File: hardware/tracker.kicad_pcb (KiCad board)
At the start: 2 copper layers, 27.9 x 40.6 mm, 19 parts, among them P1 Motor, P2 ISP, P3 Logic Power, P4 Motor Power, Q1 IRML9301TRPbF, SW1 Direction, SW2 Speed, U1 MC78L05A, U2 ATTINY85, U3 A4988

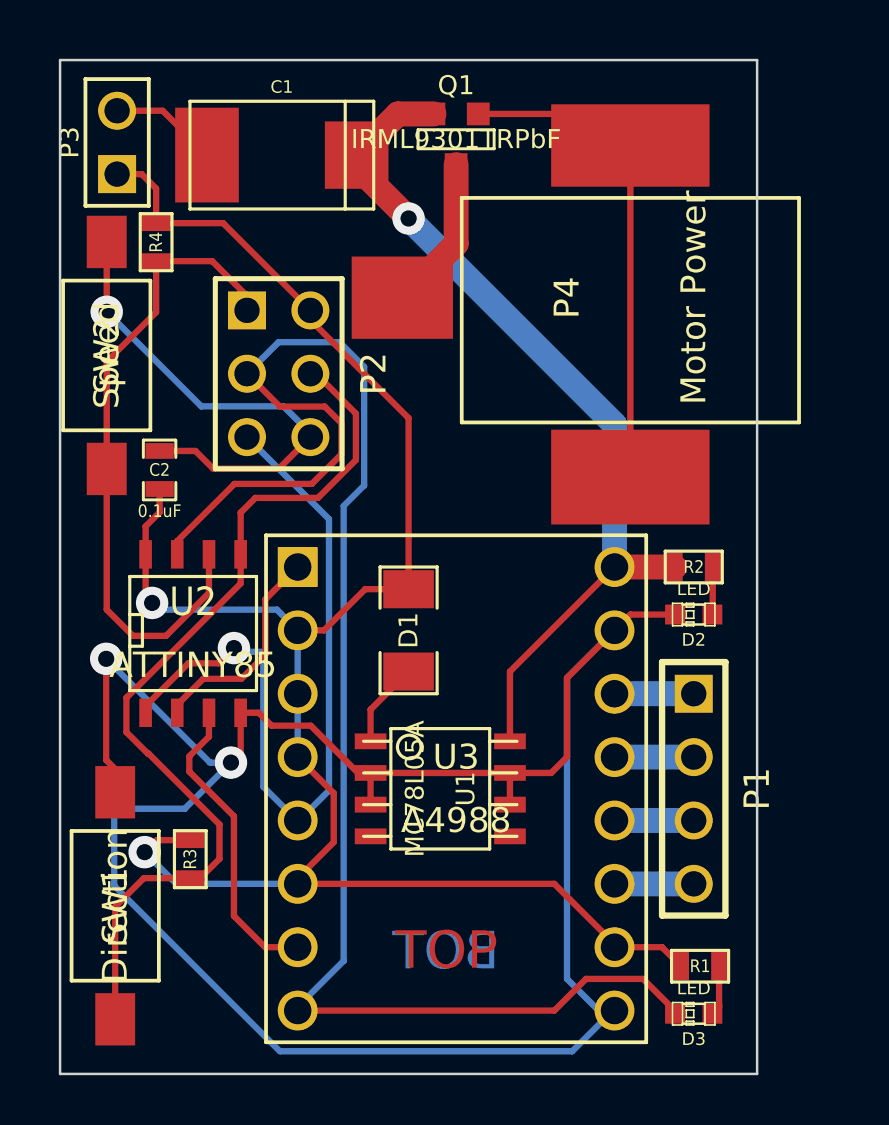
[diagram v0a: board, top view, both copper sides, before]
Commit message: move LED2 to STEP output
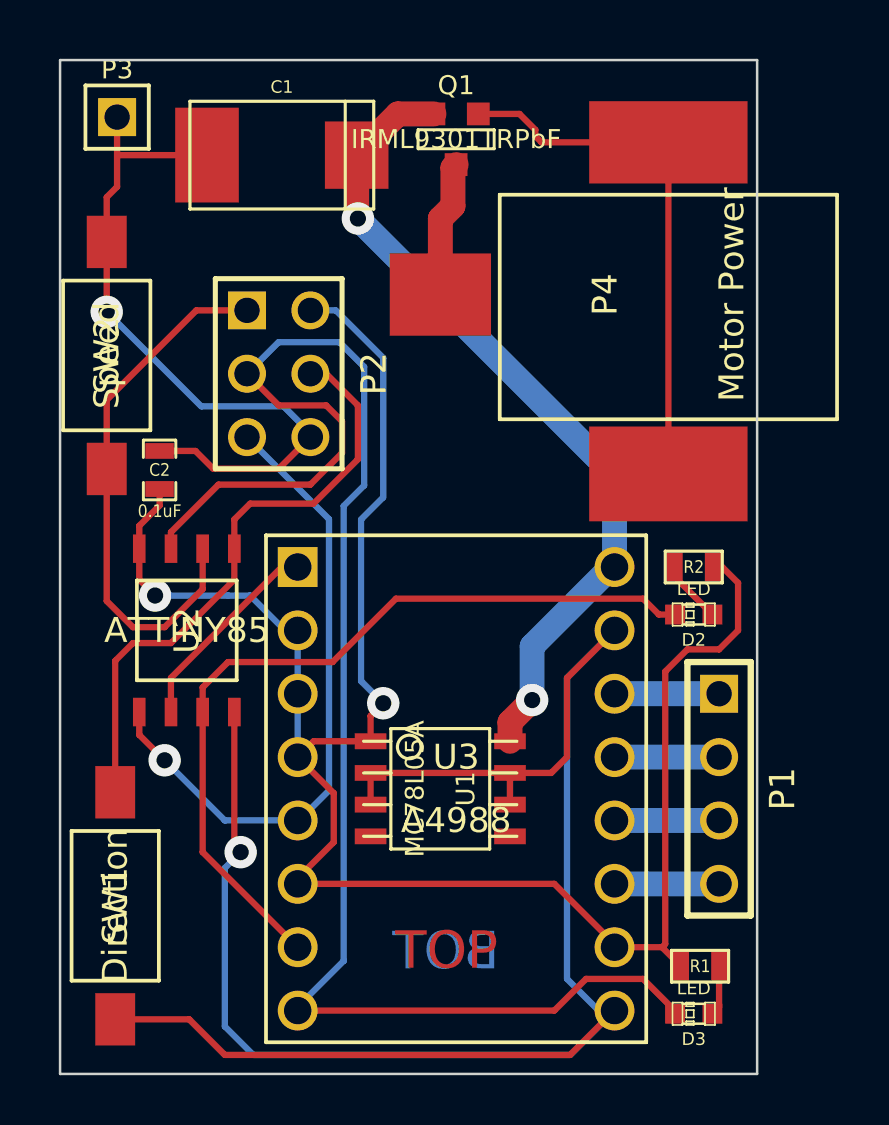
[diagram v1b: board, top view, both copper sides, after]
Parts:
- removed D1: DIODE, SM1206
- removed R3, R4: 10k, SM0603
- P3: value Logic Power -> GND; footprint PIN_ARRAY_2X1 -> PIN_ARRAY_1
- U2: footprint SO8N -> SOIC8W
- moved P4 1.53 mm to (253.0, 113.5)
- moved P1 1.02 mm to (255.0, 133.3)
- moved P3 1.02 mm to (230.9, 106.4), turned to 0 degrees
- moved U2 0.28 mm to (233.7, 127.0), turned to 90 degrees
- turned R2 to 180 degrees
- turned SW1 to 270 degrees
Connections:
- D2 pad 2: GND -> N-0000010
- P3 pad 1: +5V -> GND
- R2 pad 1: +12V -> +5V
- U1 pad 1: N-000008 (its old number) -> +5V
- U2 pad 3: N-000006 (its old number) -> N-0000010
- U3 pad 7: N-000006 (its old number) -> N-0000010
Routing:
- net N-0000010: track 0.00 -> 32.7 mm
- net N-000006: track 36.7 -> 24.3 mm
- net N-000006 (its old number): track 12.3 -> 0.00 mm
- net N-000008: track 26.4 -> 21.7 mm
- net N-000003: track 30.6 -> 26.0 mm
- net +5V: track 76.8 -> 80.4 mm
- net N-000008 (its old number): track 3.43 -> 0.00 mm
- net +12V: track 35.7 -> 33.4 mm, vias 1 -> 2
- net GND: track 133.1 -> 135.2 mm, vias 3 -> 2
- net N-0000018: track 3.18 -> 4.19 mm
- net N-0000017: track 3.18 -> 4.19 mm
- net N-0000016: track 3.18 -> 4.19 mm
- net N-0000015: track 3.18 -> 4.19 mm
- net N-000004: track 6.23 -> 5.47 mm
- net N-0000011: track 1.91 -> 2.53 mm
